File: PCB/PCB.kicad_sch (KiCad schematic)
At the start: 47 parts, among them IC1 SL2.1A, J1 USB_C_Receptacle_USB2.0_16P, J2 USB_C_Receptacle_USB2.0_16P, J3 USB_C_Receptacle_USB2.0_16P, J4 USB_C_Receptacle_USB2.0_16P, J5 AudioJack4, SW1 Mute_button, U1 PCM2902, U2 USBLC6-2SC6, U3 USBLC6-2SC6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

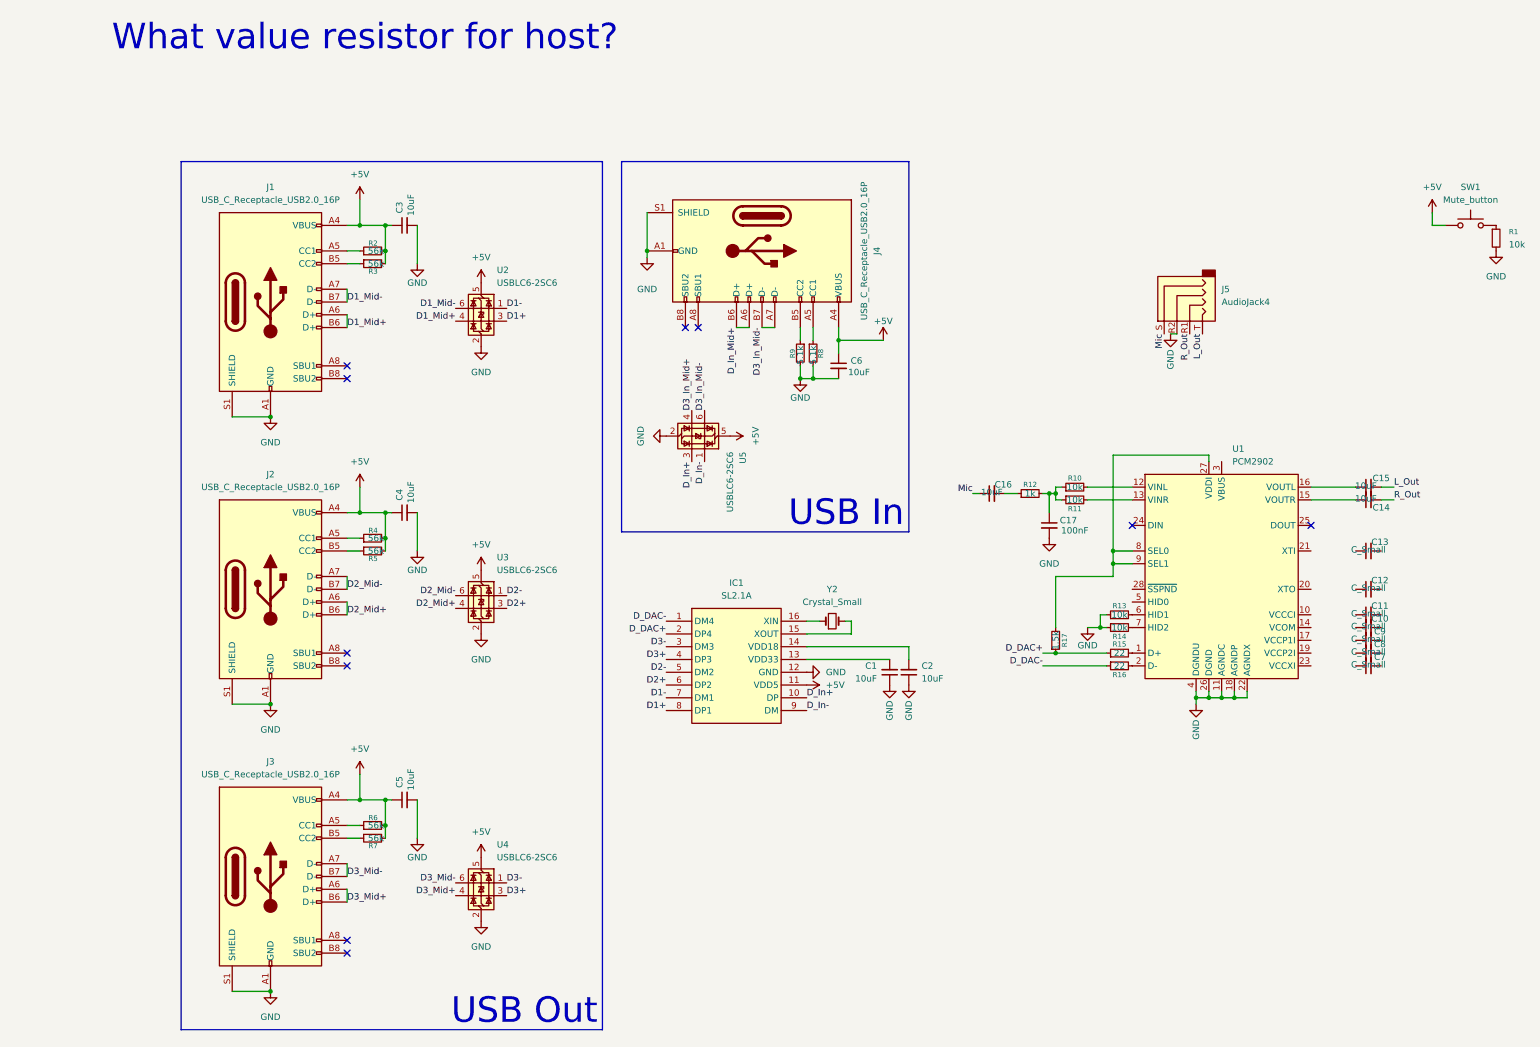
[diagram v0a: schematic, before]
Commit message: fixed schematic and routed usb hub
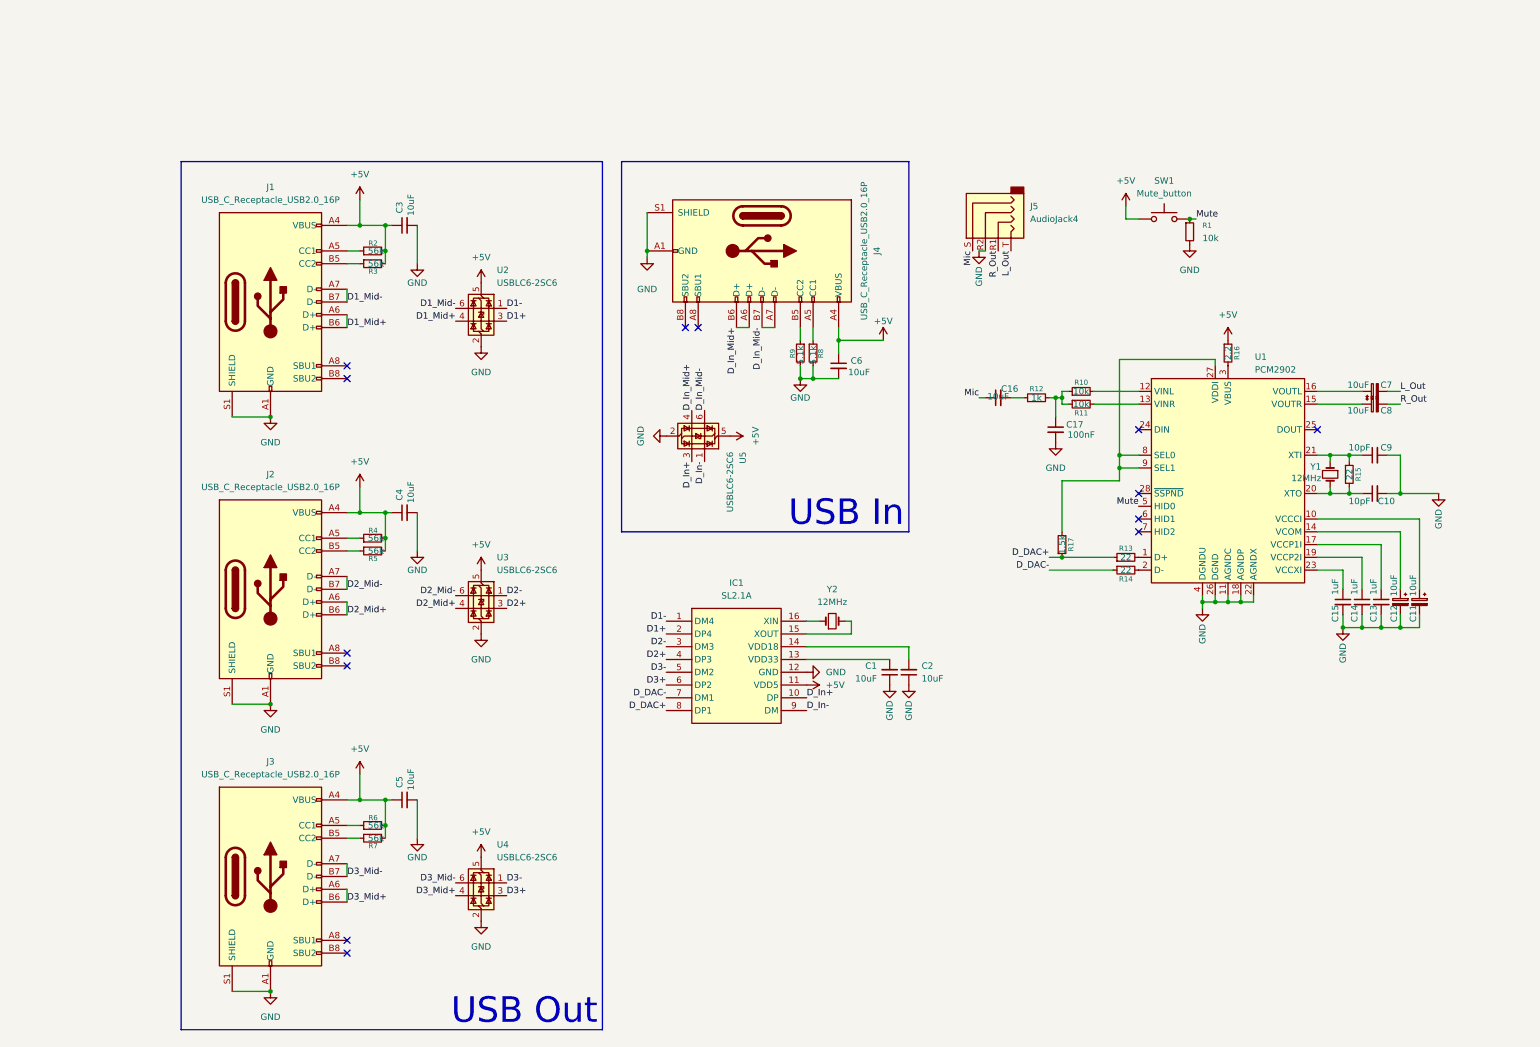
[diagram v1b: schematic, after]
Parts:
- removed C11, C12, C7, C8: C_Small, symbol Device:C_Small
- added C11, C12, C7, C8: 10uF, Capacitor_SMD:C_0805_2012Metric_Pad1.18x1.45mm_HandSolder, symbol Device:C_Polarized_Small
- added Y1: 12MHz, Crystal:Crystal_HC49-4H_Vertical, symbol Device:Crystal_Small
- C1, C16, C17, C2, C3, C4, C5, C6: footprint (none) -> Capacitor_SMD:C_0805_2012Metric_Pad1.18x1.45mm_HandSolder
- C10, C9: value C_Small -> 10pF; footprint (none) -> Capacitor_SMD:C_0805_2012Metric_Pad1.18x1.45mm_HandSolder
- C13: value C_Small -> 1uF; footprint (none) -> Capacitor_SMD:C_0805_2012Metric_Pad1.18x1.45mm_HandSolder
- C14, C15: value 10uF -> 1uF; footprint (none) -> Capacitor_SMD:C_0805_2012Metric_Pad1.18x1.45mm_HandSolder
- IC1: footprint SOIC127P604X185-16N -> Package_SO:STC_SOP-16_3.9x9.9mm_P1.27mm
- J1, J2, J3, J4: footprint (none) -> Connector_USB:USB_C_Receptacle_GCT_USB4110
- J5: footprint (none) -> Connector_Audio:Jack_3.5mm_PJ320D_Horizontal
- R1, R10, R11, R12, R15, R17, R2, R3, R4, R5, R6, R7, R8, R9: footprint (none) -> Resistor_SMD:R_0805_2012Metric_Pad1.20x1.40mm_HandSolder
- R13, R14: value 10k -> 22; footprint (none) -> Resistor_SMD:R_0805_2012Metric_Pad1.20x1.40mm_HandSolder
- R16: value 22 -> 2.2; footprint (none) -> Resistor_SMD:R_0805_2012Metric_Pad1.20x1.40mm_HandSolder
- SW1: footprint (none) -> Button_Switch_THT:SW_PUSH_6mm_H7.3mm
- Y2: value Crystal_Small -> 12MHz; footprint (none) -> Crystal:Crystal_HC49-4H_Vertical
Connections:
- net D3_In_Mid+ is gone; now on net D_In_Mid+: U5.4 (I/O2)
- net +5V: now also R16.1
- net D1+: now also IC1.2 (DP4); no longer IC1.8 (DP1)
- net D1-: now also IC1.1 (DM4); no longer IC1.7 (DM1)
- net D2+: now also IC1.4 (DP3); no longer IC1.6 (DP2)
- net D2-: now also IC1.3 (DM3); no longer IC1.5 (DM2)
- net D3+: now also IC1.6 (DP2); no longer IC1.4 (DP3)
- net D3-: now also IC1.5 (DM2); no longer IC1.3 (DM3)
- net D_DAC+: now also IC1.8 (DP1), R13.1; no longer IC1.2 (DP4), R15.1
- net D_DAC-: now also IC1.7 (DM1), R14.1; no longer IC1.1 (DM4), R16.1
- net GND: now also C10.2, C13.2, C14.2, C15.2, C9.2, C11.2, C12.2; no longer R13.1, R14.1
- net L_Out: now also C7.2; no longer C15.2
- net R_Out: now also C8.2; no longer C14.2
- net Mute: now reaches R1.1, SW1.2
- net Mute: now also U1.5 (HID0)
- net at U1.1 (D+): now also R13.2; no longer R15.2
- net at U1.10 (VCCCI): now also C11.1
- net at U1.14 (VCOM): now also C12.1
- net at U1.15 (VOUTR): now also C8.1; no longer C14.1
- net at C15.1: now also U1.23 (VCCXI); no longer U1.16 (VOUTL)
- net at U1.17 (VCCP1I): now also C13.1
- net at U1.19 (VCCP2I): now also C14.1
- net at R16.2: now also U1.3 (VBUS); no longer U1.2 (D-)
- net at U1.20 (XTO): now also C10.1, R15.2, Y1.2
- net at U1.21 (XTI): now also C9.1, R15.1, Y1.1
- net at U1.6 (HID1): no longer R13.2
- net at R14.2: now also U1.2 (D-); no longer U1.7 (HID2)
- net D3_In_Mid- renamed D_In_Mid-
- new net: C7.1, U1.16 (VOUTL)
- no-connect marks 10 -> 13
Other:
- note removed: "What value resistor for host?"
- moved on the sheet: C16, C17, J5, R1, R10, R11, R12, R13, R14, R17, SW1, U1

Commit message: finish pcb and generate gerbers
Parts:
- removed C16: 10uF, Capacitor_SMD:C_0805_2012Metric_Pad1.18x1.45mm_HandSolder, symbol Device:C_Small
- removed C17: 100nF, Capacitor_SMD:C_0805_2012Metric_Pad1.18x1.45mm_HandSolder, symbol Device:C_Small
- removed R12: 1k, Resistor_SMD:R_0805_2012Metric_Pad1.20x1.40mm_HandSolder, symbol Device:R_Small
- C11, C12, C7, C8: footprint Capacitor_SMD:C_0805_2012Metric_Pad1.18x1.45mm_HandSolder -> Capacitor_THT:C_Radial_D4.0mm_H7.0mm_P1.50mm
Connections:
- net GND: now also R10.1, R11.2
- net at U1.13 (VINR): now also R11.1; no longer R11.2
- net Mic: no longer names the net of J5.S
